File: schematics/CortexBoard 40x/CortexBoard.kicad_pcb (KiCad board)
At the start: 2 copper layers, 32 parts, among them J2 UART6 Connector, J3 Odroid Power, J4 Bodysocket, J5 LED/Switch, J7 CORTEX CLI, J8 Cortex-Power-In, J9 Cortex-Power-Out, P1 Battery, P10 XL4015, P2 BNO055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

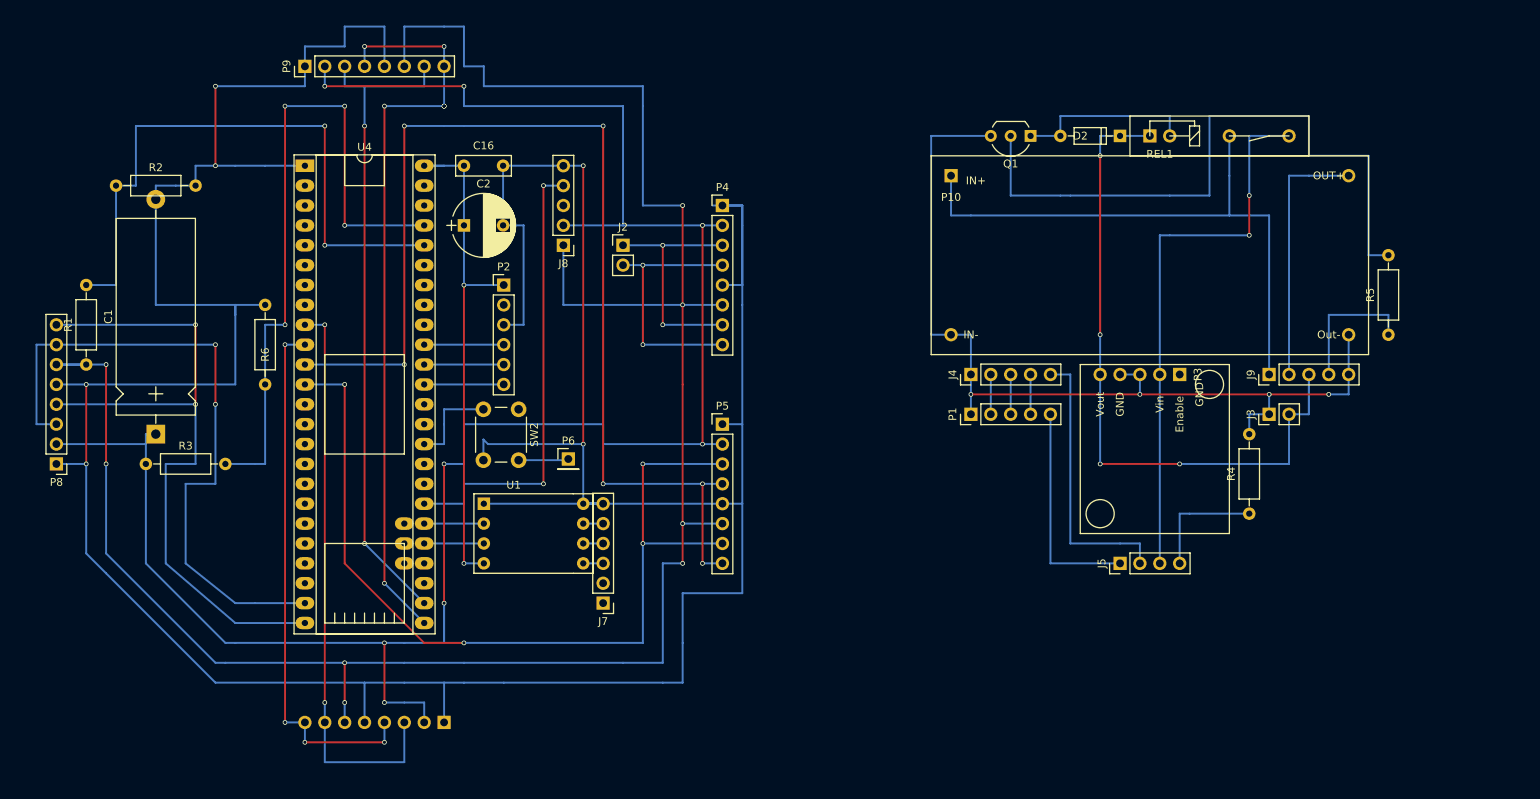
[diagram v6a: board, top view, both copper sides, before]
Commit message: Started preparation for DRS-0401 servo (already ordered)
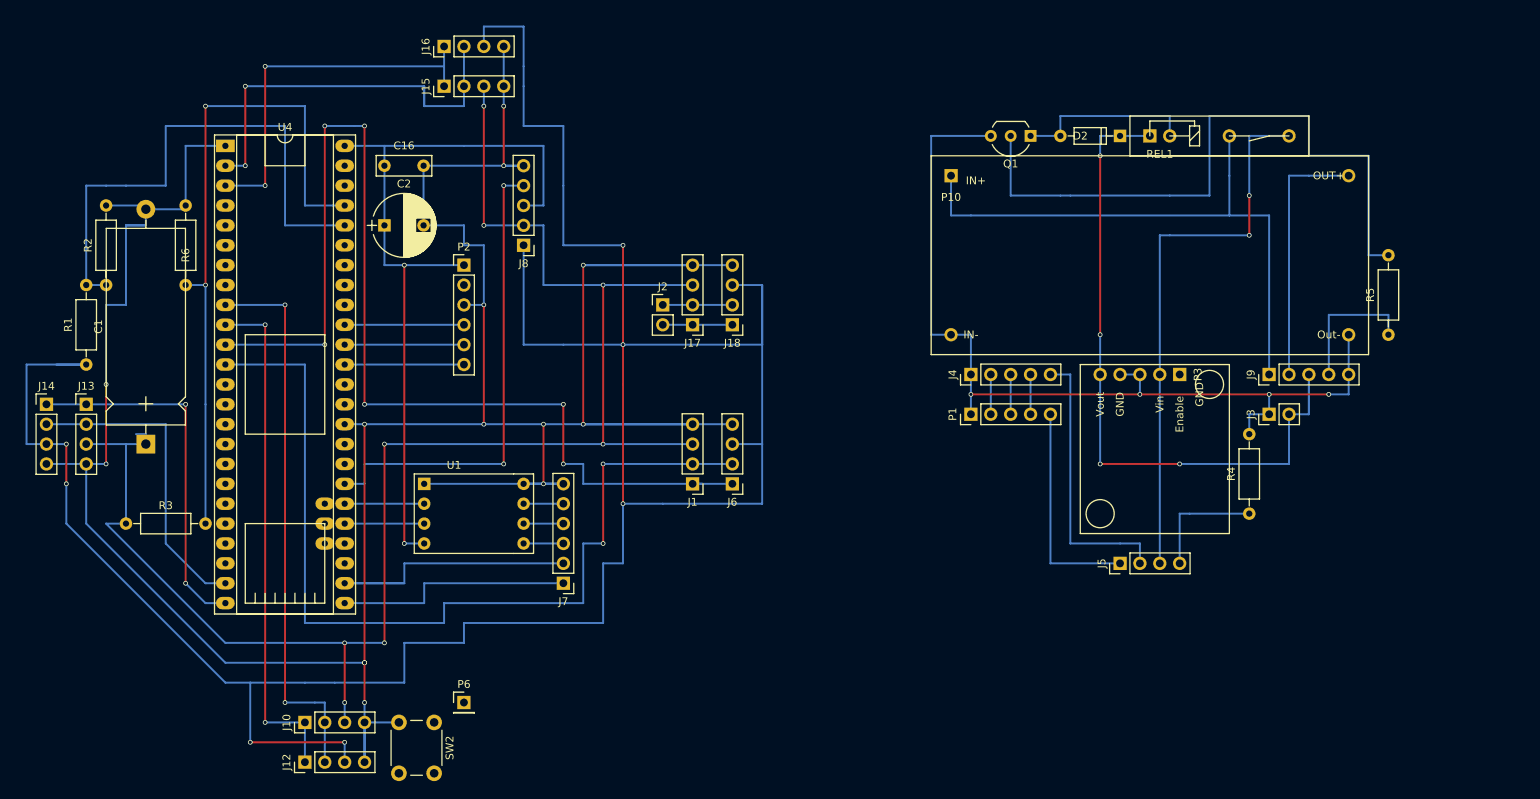
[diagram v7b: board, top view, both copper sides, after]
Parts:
- removed P4: Leg 5, Pin_Headers:Pin_Header_Straight_1x08_Pitch2.54mm
- removed P5: Leg 1, Pin_Headers:Pin_Header_Straight_1x08_Pitch2.54mm
- removed P7: Leg 2, Pin_Headers:Pin_Header_Straight_1x08_Pitch2.54mm
- removed P8: Leg 3, Pin_Headers:Pin_Header_Straight_1x08_Pitch2.54mm
- removed P9: Leg 4, Pin_Headers:Pin_Header_Straight_1x08_Pitch2.54mm
- added J1: LEG1-LO, Pin_Headers:Pin_Header_Straight_1x04_Pitch2.54mm, F.Cu at (142.2, 110.5)
- added J10: LEG2-LO, Pin_Headers:Pin_Header_Straight_1x04_Pitch2.54mm, F.Cu at (92.7, 141.0)
- added J12: LEG2-HI, Pin_Headers:Pin_Header_Straight_1x04_Pitch2.54mm, F.Cu at (92.7, 146.1)
- added J13: LEG3-LO, Pin_Headers:Pin_Header_Straight_1x04_Pitch2.54mm, F.Cu at (64.8, 100.3)
- added J14: LEG3-HI, Pin_Headers:Pin_Header_Straight_1x04_Pitch2.54mm, F.Cu at (59.7, 100.3)
- added J15: LEG4-LO, Pin_Headers:Pin_Header_Straight_1x04_Pitch2.54mm, F.Cu at (110.5, 59.7)
- added J16: LEG4-HI, Pin_Headers:Pin_Header_Straight_1x04_Pitch2.54mm, F.Cu at (110.5, 54.6)
- added J17: LEG5-LO, Pin_Headers:Pin_Header_Straight_1x04_Pitch2.54mm, F.Cu at (142.2, 90.2)
- added J18: LEG5-HI, Pin_Headers:Pin_Header_Straight_1x04_Pitch2.54mm, F.Cu at (147.3, 90.2)
- added J6: LEG1-HI, Pin_Headers:Pin_Header_Straight_1x04_Pitch2.54mm, F.Cu at (147.3, 110.5)
- moved SW2 41.4 mm to (109.2, 141.0)
- moved P6 33.9 mm to (113.0, 138.4)
- moved R6 16.3 mm to (77.5, 85.1)
- moved R2 12.8 mm to (67.3, 85.1), turned to 90 degrees
- moved U4 10.5 mm to (82.5, 67.3)
- moved C16 10.2 mm to (102.9, 69.8)
- moved C2 10.2 mm to (102.9, 77.5)
- moved J2 9.16 mm to (138.4, 87.6)
- moved R3 8.03 mm to (69.8, 115.6)
- moved U1 8.03 mm to (108.0, 110.5)
- moved J7 5.68 mm to (125.7, 123.2)
- moved P2 5.68 mm to (113.0, 82.5)
- moved J8 5.08 mm to (120.7, 80.0)
- moved C1 1.80 mm to (72.4, 105.4)
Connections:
- J7 pad 1: Net-(J7-Pad1) -> /TX5
- J7 pad 2: /RX -> /RX5
- U4 pad 2: /RX -> /TX1
- U4 pad 25: /RX5 -> /TX5
- U4 pad 26: /TX5 -> /RX5
- U4 pad 3: Net-(J7-Pad1) -> /RX1
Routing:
- net /+14V: track 276.3 -> 346.9 mm, vias 8 -> 7
- net /GND: track 488.0 -> 419.6 mm, vias 6 -> 15
- net /RX5: track 98.6 -> 38.1 mm, vias 6 -> 1
- net /TX5: track 84.4 -> 30.5 mm, vias 2 -> 0
- net /TX1: track 0.00 -> 53.3 mm, vias 0 -> 2
- net /RX1: track 0.00 -> 48.3 mm, vias 0 -> 2
- net /TX4: track 84.7 -> 40.6 mm, vias 2 -> 0
- net /RX4: track 91.1 -> 47.4 mm
- net /+10V: track 264.6 -> 227.3 mm
- net Net-(R1-Pad2): track 103.5 -> 69.2 mm, vias 2 -> 0
- net /VIn+5V: track 66.0 -> 99.1 mm
- net /RX6: track 33.0 -> 8.89 mm, vias 3 -> 0
- net /TX6: track 30.5 -> 8.89 mm, vias 2 -> 1
- net Net-(P6-Pad1): track 6.41 -> 0.00 mm
- net /SDA: track 10.2 -> 15.2 mm
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
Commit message: first try with DRS-0401 PCB
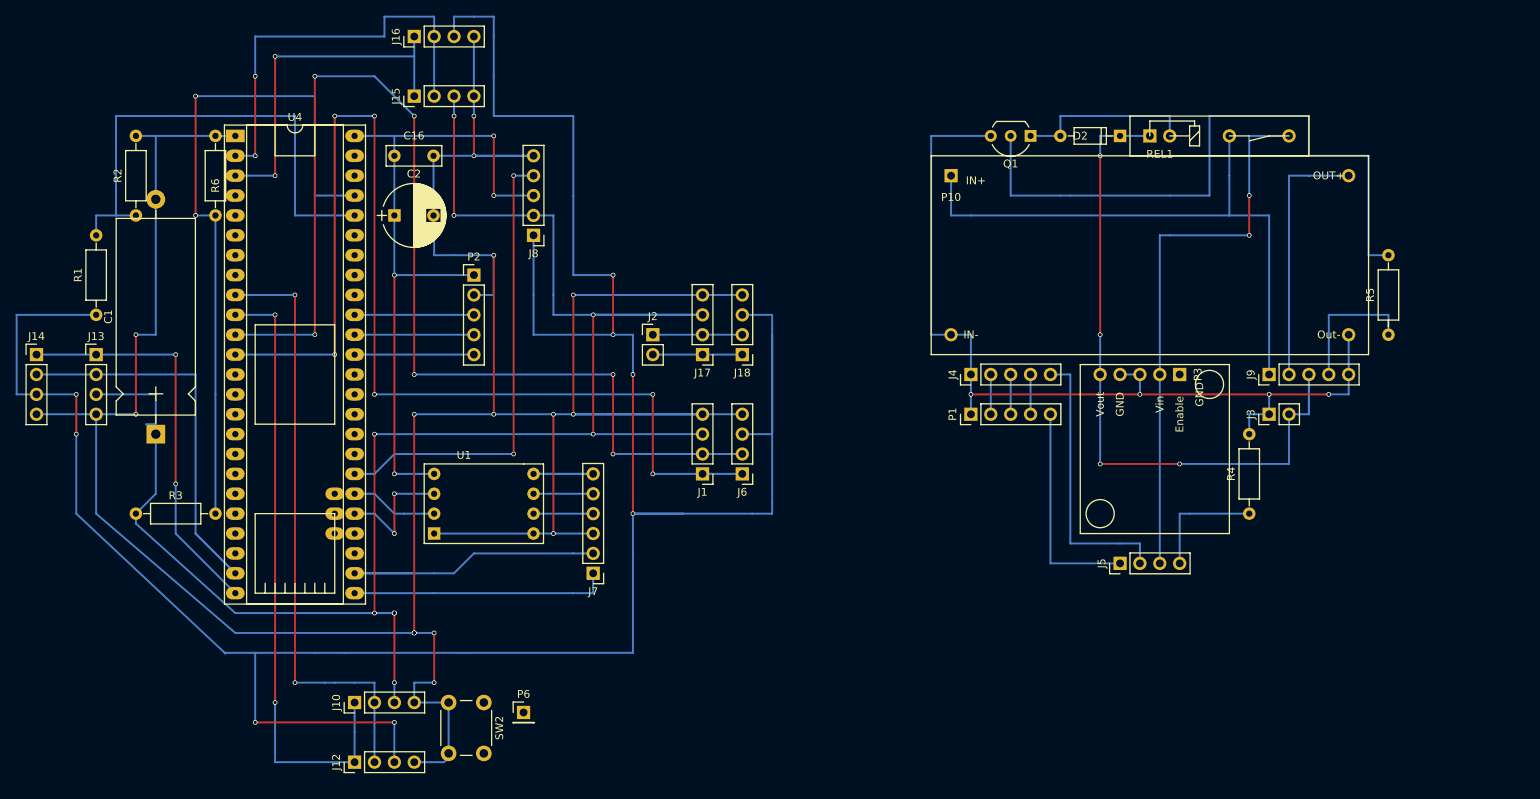
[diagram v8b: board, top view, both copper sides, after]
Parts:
- P2: footprint Pin_Headers:Pin_Header_Straight_1x06_Pitch2.54mm -> Pin_Headers:Pin_Header_Straight_1x05_Pitch2.54mm
- moved R2 9.67 mm to (71.1, 76.2)
- moved R6 9.67 mm to (81.3, 76.2)
- moved P6 7.73 mm to (120.7, 139.7)
- moved J10 6.84 mm to (99.1, 138.4)
- moved SW2 6.84 mm to (115.6, 138.4)
- moved J13 6.48 mm to (66.0, 94.0)
- moved R1 6.48 mm to (66.0, 88.9)
- moved J14 6.48 mm to (58.4, 94.0)
- moved J12 6.35 mm to (99.1, 146.1)
- moved J18 4.02 mm to (148.6, 94.0)
- moved J2 4.02 mm to (137.2, 91.4)
- moved J17 4.02 mm to (143.5, 94.0)
- moved J15 4.02 mm to (106.7, 61.0)
- moved J16 4.02 mm to (106.7, 53.3)
- moved J7 4.02 mm to (129.5, 121.9)
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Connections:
- J7 pad 3: /3.3V_ODroid -> /GND
- J7 pad 4: /SCL-ODroid -> /SDA-ODroid
- J7 pad 5: /SDA-ODroid -> /SCL-ODroid
- J7 pad 6: /GND -> /3.3V_ODroid
- P2 pad 2: (no net) -> /GND
- P2 pad 3: /GND -> /SDA
- P2 pad 4: /SDA -> /SCL
- P2 pad 5: /SCL -> /RST
- U4 pad 11: /RX2 -> /TX2
- U4 pad 12: /TX2 -> /RX2
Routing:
- net /TX2: track 118.1 -> 154.5 mm, vias 2 -> 6
- net /+10V: track 227.3 -> 246.7 mm, vias 8 -> 9
- net /+14V: track 346.9 -> 365.5 mm, vias 7 -> 8
- net /3.3V_ODroid: track 5.08 -> 22.9 mm
- net /TX4: track 40.6 -> 55.4 mm
- net /RX3: track 66.0 -> 80.0 mm
- net /VIn+5V: track 99.1 -> 89.0 mm, vias 2 -> 5
- net /TX3: track 71.1 -> 77.5 mm
- net /SCL0: track 10.2 -> 16.3 mm, vias 0 -> 2
- net /GND: track 419.6 -> 413.7 mm, vias 15 -> 16
- net Net-(R1-Pad2): track 69.2 -> 64.1 mm
- net /RX4: track 47.4 -> 52.1 mm
- net /RX2: track 141.0 -> 143.5 mm
- net /TX6: track 8.89 -> 11.4 mm
- net /RX6: track 8.89 -> 11.4 mm
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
